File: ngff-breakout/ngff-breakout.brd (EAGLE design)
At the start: 70 x 70 mm, 43 parts, among them K1 694108106102, U1 IP4234CZ6, U2 LD1085D2T33R, X1 MPCIE-JAE, X2 MINI-USB-SHIELD-UX60-MB-5ST

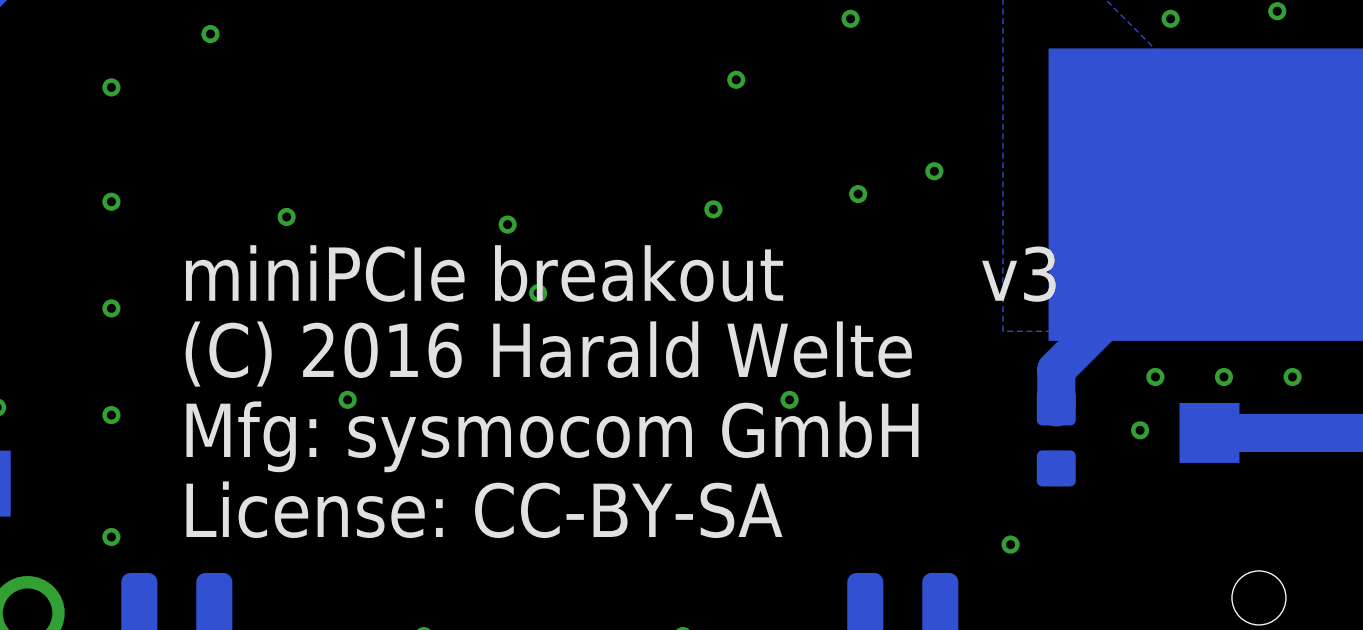
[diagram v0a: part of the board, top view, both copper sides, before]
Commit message: ngff-breakout: Rename "mPCIe" -> "NGFF WWAN" and re-start version at v1
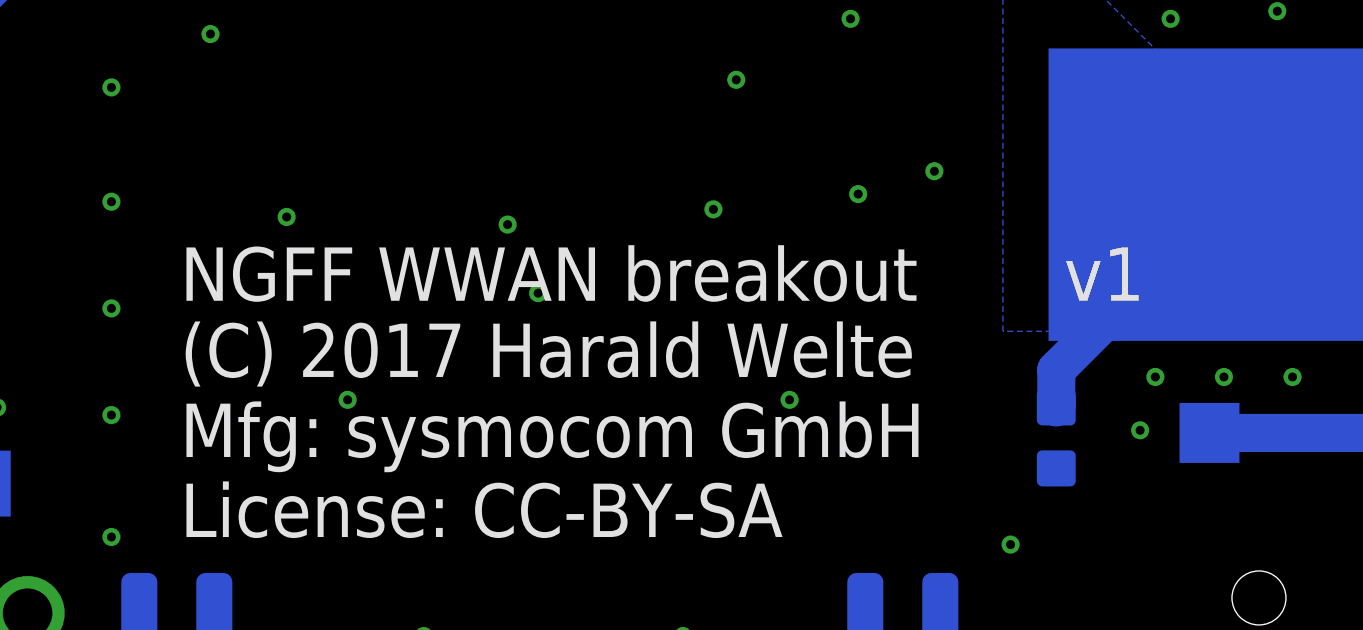
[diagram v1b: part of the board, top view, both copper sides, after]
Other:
- board text added: "(C) 2017 Harald Welte Mfg: sysmocom GmbH License: CC-BY-SA"
- board text added: "NGFF WWAN breakout"
- board text removed: "(C) 2016 Harald Welte Mfg: sysmocom GmbH License: CC-BY-SA"
- board text removed: "miniPCIe breakout"
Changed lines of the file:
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@@
 <wire x1="50" y1="70" x2="-20" y2="70" width="0" layer="20"/>
 <wire x1="-20" y1="70" x2="-20" y2="0" width="0" layer="20"/>
-<text x="4.318" y="17.78" size="1.778" layer="25" font="vector">miniPCIe breakout</text>
-<text x="4.318" y="9.906" size="1.778" layer="25" font="vector">(C) 2016 Harald Welte
+<text x="4.318" y="17.78" size="1.778" layer="25" font="vector">NGFF WWAN breakout</text>
+<text x="4.318" y="9.906" size="1.778" layer="25" font="vector">(C) 2017 Harald Welte
 Mfg: sysmocom GmbH
 License: CC-BY-SA</text>
-<text x="30.988" y="17.78" size="1.778" layer="25" font="vector">&gt;VERSION</text>
-<text x="18.796" y="5.588" size="1.778" layer="26" font="vector" rot="MR90">miniPCIe breakout</text>
-<text x="10.668" y="5.588" size="1.778" layer="26" font="vector" rot="MR90">(C) 2016 Harald Welte
+<text x="33.782" y="17.78" size="1.778" layer="25" font="vector">&gt;VERSION</text>
+<text x="18.796" y="5.588" size="1.778" layer="26" font="vector" rot="MR90">NGFF WWAN breakout</text>
+<text x="10.668" y="5.588" size="1.778" layer="26" font="vector" rot="MR90">(C) 2017 Harald Welte
 Mfg: sysmocom GmbH
 License: CC-BY-SA</text>
-<text x="18.796" y="32.004" size="1.778" layer="26" font="vector" rot="MR90">&gt;VERSION</text>
+<text x="18.796" y="34.798" size="1.778" layer="26" font="vector" rot="MR90">&gt;VERSION</text>
 <text x="1.6575" y="61.8375" size="1.778" layer="22" font="vector" ratio="10" rot="MR90">1</text>
 <text x="47.498" y="36.068" size="1.4224" layer="26" font="vector" ratio="14" rot="MR90">USB</text>
@@
 </plain>
 <attributes>
-<attribute name="VERSION" value="v3"/>
+<attribute name="VERSION" value="v1"/>
 </attributes>
 <variantdefs>

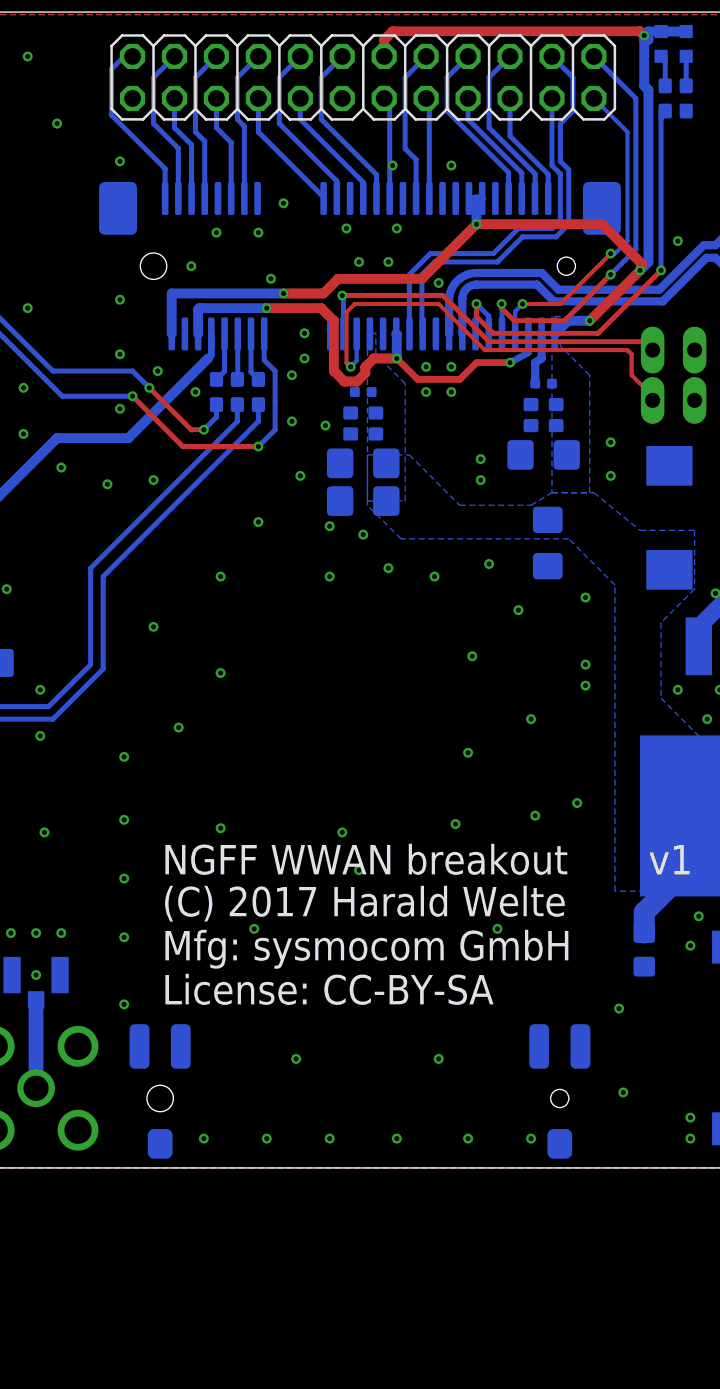
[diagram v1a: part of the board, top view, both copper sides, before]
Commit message: ngff-breakout: Partial migration over to NGFF
The mPCIe slot has been removed and the NGFF slot added. Basic
connections have been made in the schematics, but it's far from being
complete.  No effort on the PCB routing has been made so far.
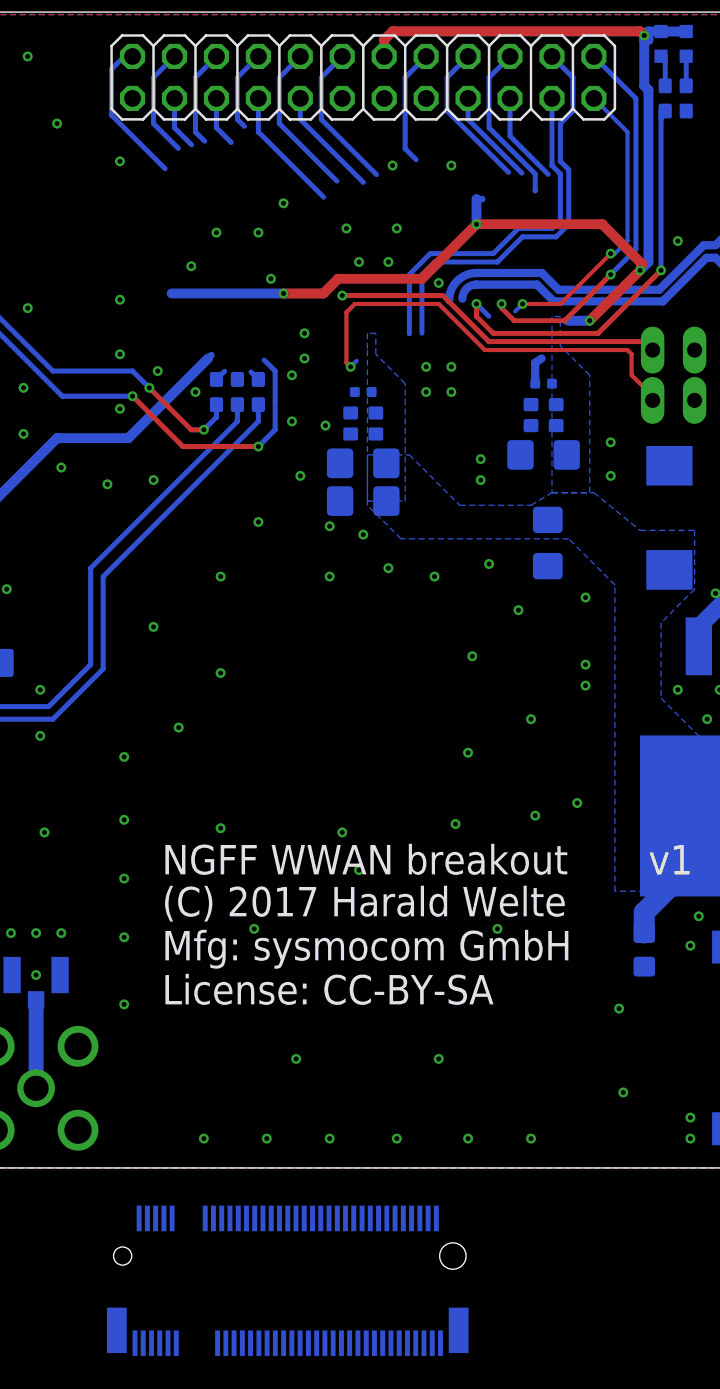
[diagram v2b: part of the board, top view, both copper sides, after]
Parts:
- removed X1: MPCIE-JAE, con-miniPCIe:MM60-52
- added NGFF1: NGFF_B, con-ngff:NGFF_B_AMP
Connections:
- removed net VDD_1V5: X1.28, X1.48, X1.6
- net !CLKREQ: no longer X1.7
- net COEX1: now also NGFF1.64; no longer X1.3
- net COEX2: now also NGFF1.62; no longer X1.5
- net GND: now also NGFF1.11, NGFF1.27, NGFF1.3, NGFF1.33, NGFF1.39, NGFF1.5, NGFF1.51, NGFF1.57, NGFF1.71, NGFF1.73; no longer X1.15, X1.18, X1.21, X1.26, X1.27, X1.29, X1.34, X1.35, X1.37, X1.4, X1.40, X1.43, X1.50, X1.9
- net LED_WLAN: no longer X1.44
- net LED_WPAN: no longer X1.46
- net N$3: no longer X1.42
- net N$5: now also NGFF1.34; no longer X1.10
- net N$8: now also NGFF1.32; no longer X1.12
- net N$9: now also NGFF1.30; no longer X1.14
- net PERN0: no longer X1.23
- net PERP0: no longer X1.25
- net PERST: now also NGFF1.67; no longer X1.22
- net PETN0: no longer X1.31
- net PETP0: no longer X1.33
- net REFCLK+: no longer X1.13
- net REFCLK-: no longer X1.11
- net RSVRD45: no longer X1.45
- net RSVRD47: no longer X1.47
- net RSVRD49: no longer X1.49
- net RSVRD51: no longer X1.51
- net SMB_CLK: now also NGFF1.58; no longer X1.30
- net SMB_DATA: now also NGFF1.56; no longer X1.32
- net UIM_C4: no longer X1.19
- net UIM_C8: no longer X1.17
- net USB_D_N: now also NGFF1.9; no longer X1.36
- net USB_D_P: now also NGFF1.7; no longer X1.38
- net USIM_POWER: now also NGFF1.36; no longer X1.8
- net USIM_VPP: no longer X1.16
- net VCC_3V3: now also NGFF1.2, NGFF1.4, NGFF1.70, NGFF1.72, NGFF1.74; no longer X1.2, X1.24, X1.39, X1.41, X1.52
- net WAKE: now also NGFF1.23; no longer X1.1
- net W_DISABLE: now also NGFF1.8; no longer X1.20
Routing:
- net VDD_1V5: track 29.7 -> 0.00 mm, vias 3 -> 0
- net GND: track 26.3 -> 19.1 mm
- net PETP0: track 6.14 -> 0.27 mm
- net VCC_3V3: track 87.7 -> 83.3 mm
- net REFCLK+: track 9.30 -> 4.93 mm
- net !CLKREQ: track 9.36 -> 5.89 mm
- net REFCLK-: track 6.43 -> 3.04 mm
- net COEX2: track 6.49 -> 3.24 mm
- net COEX1: track 9.75 -> 6.71 mm
- net N$8: track 2.77 -> 0.03 mm
- net PETN0: track 9.40 -> 7.05 mm
- net N$9: track 2.94 -> 0.63 mm
- net N$5: track 2.96 -> 0.70 mm
- net W_DISABLE: track 22.5 -> 20.3 mm
- net USB_D_P: track 20.4 -> 18.3 mm
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
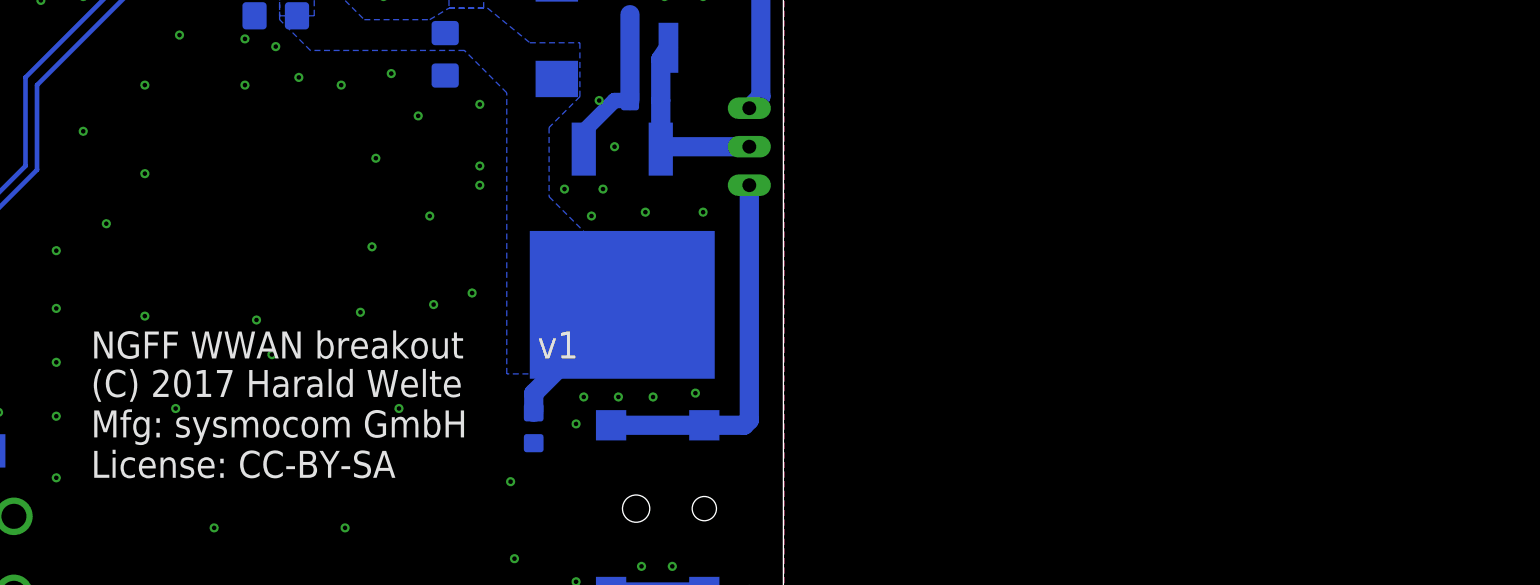
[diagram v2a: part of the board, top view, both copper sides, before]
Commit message: ngff-breakout: make 4layer PCB
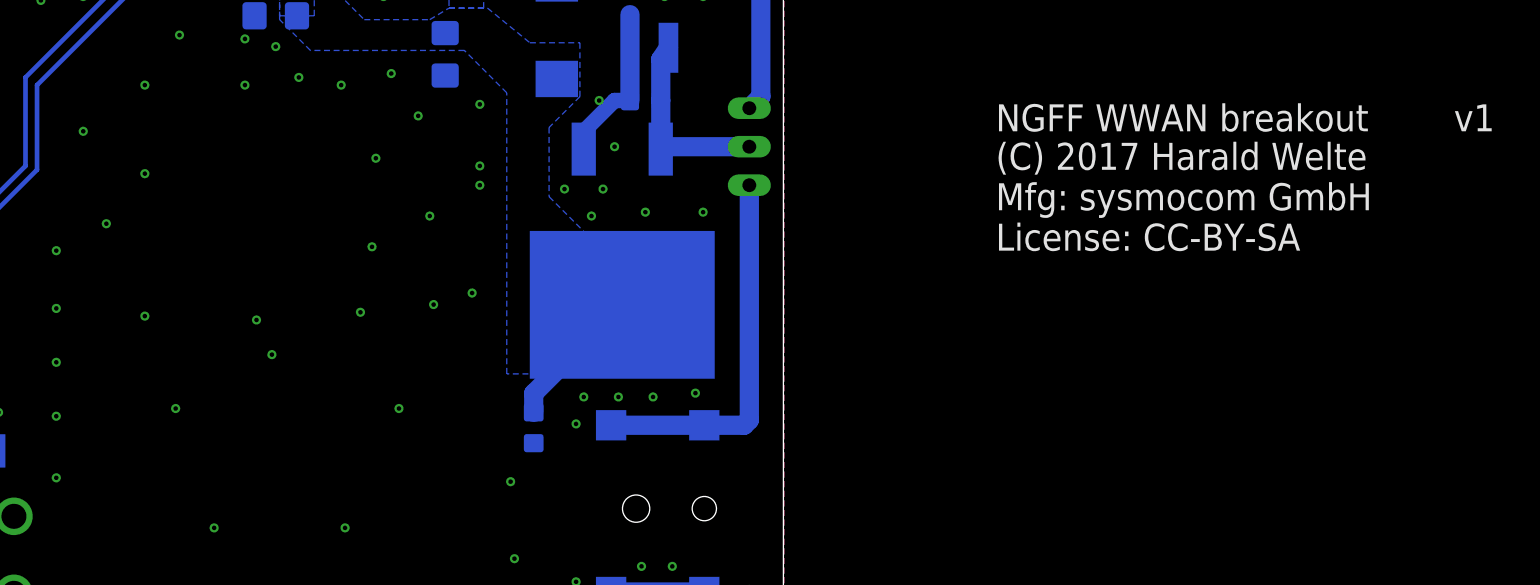
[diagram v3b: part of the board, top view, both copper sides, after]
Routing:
- added copper zone on layer 2, net GND
- added copper zone on layer 15, net N$6
